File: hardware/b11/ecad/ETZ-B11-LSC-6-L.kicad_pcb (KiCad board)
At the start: 2 copper layers, 131.5 x 85.8 mm, 44 parts, among them SW1 Kailh_socket_PG1350, SW10 Kailh_socket_PG1350, SW11 Kailh_socket_PG1350, SW12 Kailh_socket_PG1350, SW13 Kailh_socket_PG1350, SW14 Kailh_socket_PG1350, SW15 Kailh_socket_PG1350, SW16 Kailh_socket_PG1350, SW17 Kailh_socket_PG1350, SW18 Kailh_socket_PG1350, SW19 Kailh_socket_PG1350, SW2 Kailh_socket_PG1350, SW20 Kailh_socket_PG1350, SW21 Kailh_socket_PG1350, SW22 Kailh_socket_PG1350, SW3 Kailh_socket_PG1350, SW4 Kailh_socket_PG1350, SW5 Kailh_socket_PG1350, SW6 Kailh_socket_PG1350, SW7 Kailh_socket_PG1350, SW8 Kailh_socket_PG1350, SW9 Kailh_socket_PG1350

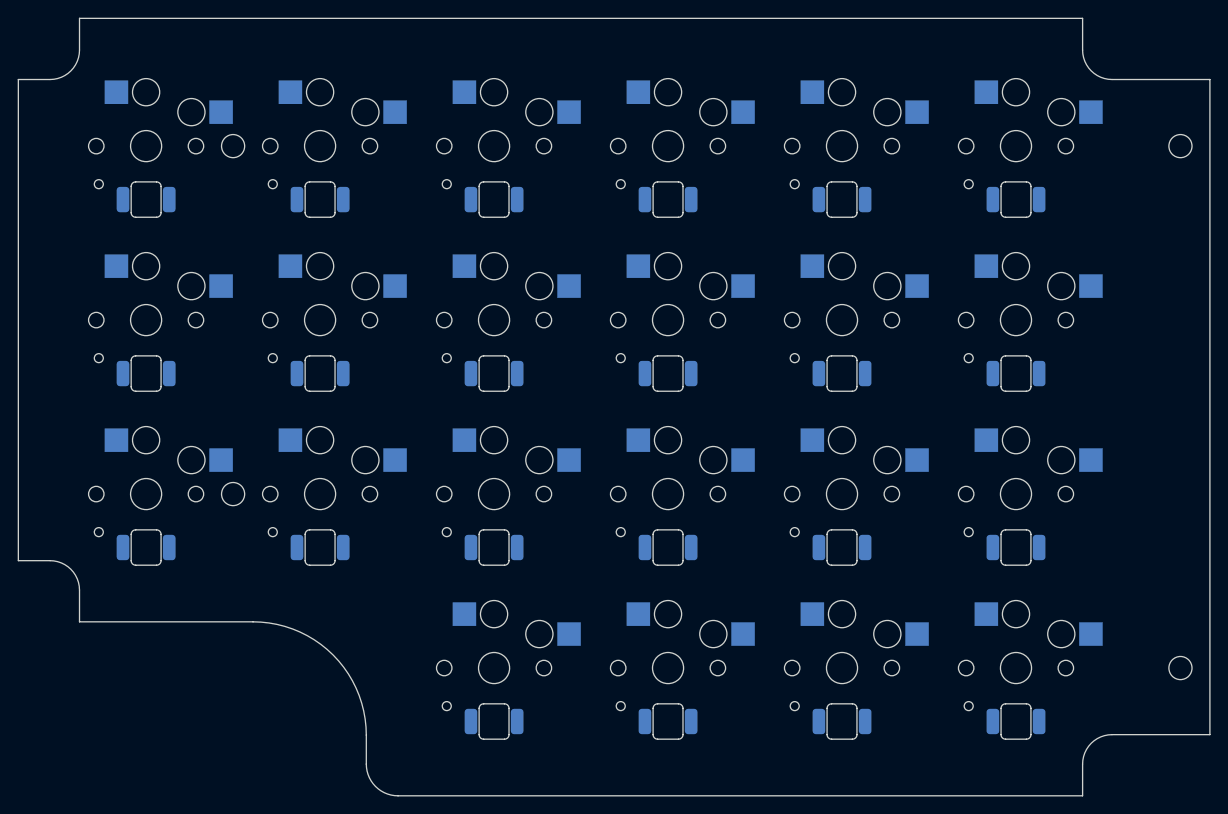
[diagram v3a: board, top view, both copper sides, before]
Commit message: fix(hardware/b11): fix switch socket placement, 3D models, and submodule pins
- Pin MX_V2 submodule to ab59b57 (before upstream "topside pads" change that
  moved SMD pads to F.Cu — old commit has correct B.Cu pads natively)
- Fix SWIG type-registry corruption in both switch placement scripts by
  pre-loading all footprint instances and caching pad refs before LoadBoard()
- Fix LP script: add make_patched_lib to rewrite Choc socket 3D model path
  to absolute path and convert old (at ...) inch offset to (offset ...) mm
  format — KiCad 9 was multiplying the old format by 25.4, placing model
  127mm off-center
- Regenerate all 8 carrier PCBs with updated board outlines (LSC-6 mounting
  hole positions) and correctly placed switches + LEDs

Co-Authored-By: Claude Sonnet 4.6 <noreply@anthropic.com>
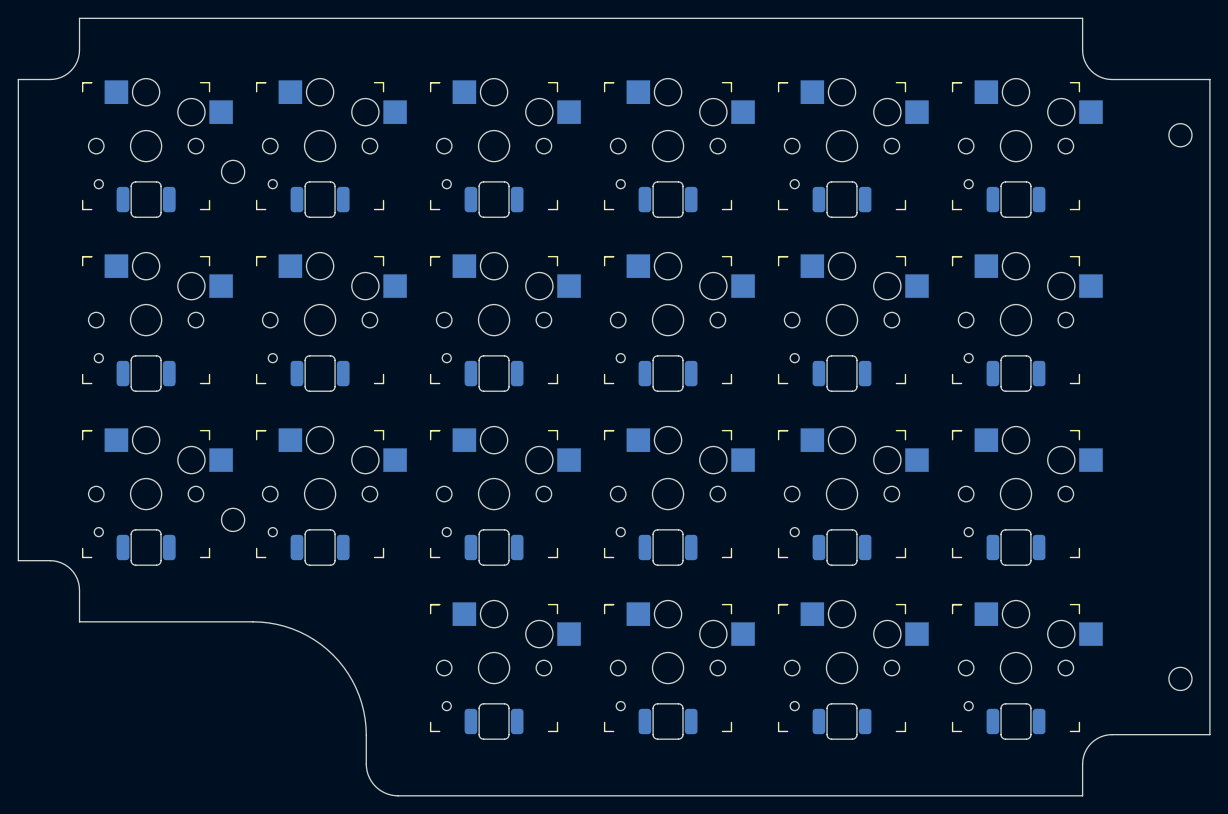
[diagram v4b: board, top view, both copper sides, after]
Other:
- outline, holes or cut-outs redrawn

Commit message: fix(hardware/b11): adjust LED offset to 5.0mm and regenerate all carrier PCBs
Reduces south-facing LED offset from 5.9mm to 5.0mm (closer to the
standard 5.08mm switch-to-LED spacing). All 8 carrier PCBs regenerated.

Co-Authored-By: Claude Sonnet 4.6 <noreply@anthropic.com>
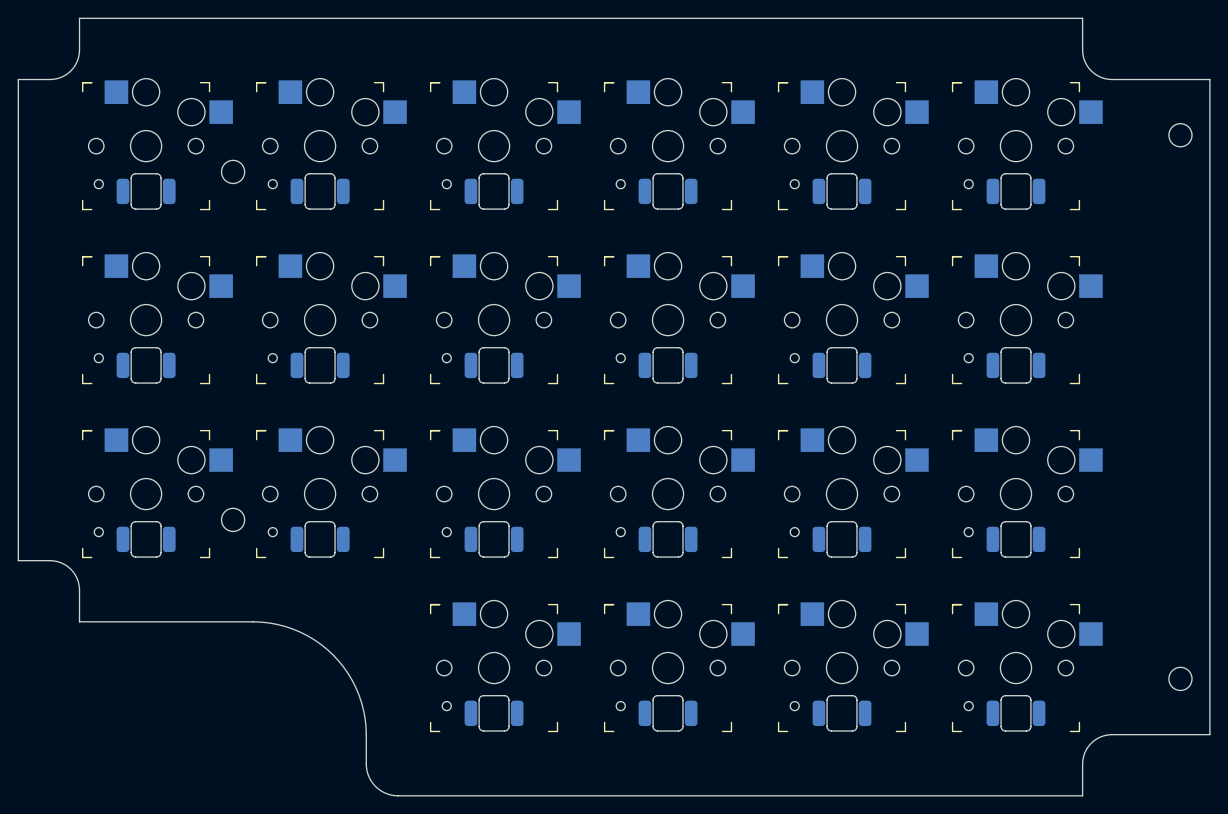
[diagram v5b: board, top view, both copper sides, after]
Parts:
- moved LED13 0.90 mm to (96.8, 116.7)
- moved LED14 0.90 mm to (116.0, 116.7)
- moved LED15 0.90 mm to (135.2, 116.7)
- moved LED16 0.90 mm to (154.4, 116.7)
- moved LED17 0.90 mm to (173.6, 116.7)
- moved LED18 0.90 mm to (192.8, 116.7)
- moved LED1 0.90 mm to (96.8, 78.3)
- moved LED10 0.90 mm to (154.4, 97.5)
- moved LED11 0.90 mm to (173.6, 97.5)
- moved LED12 0.90 mm to (192.8, 97.5)
- moved LED19 0.90 mm to (135.2, 135.9)
- moved LED2 0.90 mm to (116.0, 78.3)
- moved LED20 0.90 mm to (154.4, 135.9)
- moved LED21 0.90 mm to (173.6, 135.9)
- moved LED22 0.90 mm to (192.8, 135.9)
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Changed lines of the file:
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@@
 	(footprint "LED_SMD_6028_BackMount"
 		(layer "B.Cu")
-		(at 135.25 117.6)
+		(at 135.25 116.699999)
 		(descr "SMD 6028 back-paste reverse-mount LED, 5.88x2.80mm body, 3.20mm lens, slot 3.3x6.2mm")
 		(tags "LED SMD 6028 reverse-mount back-paste backlighting Choc")
@@
 	(footprint "LED_SMD_6028_BackMount"
 		(layer "B.Cu")
-		(at 135.25 98.4)
+		(at 135.25 78.3)
 		(descr "SMD 6028 back-paste reverse-mount LED, 5.88x2.80mm body, 3.20mm lens, slot 3.3x6.2mm")
 		(tags "LED SMD 6028 reverse-mount back-paste backlighting Choc")
-		(property "Reference" "LED9"
+		(property "Reference" "LED3"
 			(at 0 -2 0)
 			(layer "B.Fab")
@@
 	(footprint "LED_SMD_6028_BackMount"
 		(layer "B.Cu")
-		(at 96.85 98.4)
+		(at 192.85 135.899999)
 		(descr "SMD 6028 back-paste reverse-mount LED, 5.88x2.80mm body, 3.20mm lens, slot 3.3x6.2mm")
 		(tags "LED SMD 6028 reverse-mount back-paste backlighting Choc")
-		(property "Reference" "LED7"
+		(property "Reference" "LED22"
 			(at 0 -2 0)
 			(layer "B.Fab")
@@
 	(footprint "LED_SMD_6028_BackMount"
 		(layer "B.Cu")
-		(at 173.649999 117.6)
+		(at 173.649999 78.3)
 		(descr "SMD 6028 back-paste reverse-mount LED, 5.88x2.80mm body, 3.20mm lens, slot 3.3x6.2mm")
 		(tags "LED SMD 6028 reverse-mount back-paste backlighting Choc")
-		(property "Reference" "LED17"
+		(property "Reference" "LED5"
 			(at 0 -2 0)
 			(layer "B.Fab")
@@
 	(footprint "LED_SMD_6028_BackMount"
 		(layer "B.Cu")
-		(at 173.649999 136.799999)
+		(at 116.05 97.5)
 		(descr "SMD 6028 back-paste reverse-mount LED, 5.88x2.80mm body, 3.20mm lens, slot 3.3x6.2mm")
 		(tags "LED SMD 6028 reverse-mount back-paste backlighting Choc")
-		(property "Reference" "LED21"
+		(property "Reference" "LED8"
 			(at 0 -2 0)
 			(layer "B.Fab")
@@
 	(footprint "LED_SMD_6028_BackMount"
 		(layer "B.Cu")
-		(at 192.85 136.799999)
+		(at 116.05 78.3)
 		(descr "SMD 6028 back-paste reverse-mount LED, 5.88x2.80mm body, 3.20mm lens, slot 3.3x6.2mm")
 		(tags "LED SMD 6028 reverse-mount back-paste backlighting Choc")
-		(property "Reference" "LED22"
+		(property "Reference" "LED2"
 			(at 0 -2 0)
 			(layer "B.Fab")
@@
 	(footprint "LED_SMD_6028_BackMount"
 		(layer "B.Cu")
-		(at 192.85 79.2)
+		(at 173.649999 97.5)
 		(descr "SMD 6028 back-paste reverse-mount LED, 5.88x2.80mm body, 3.20mm lens, slot 3.3x6.2mm")
 		(tags "LED SMD 6028 reverse-mount back-paste backlighting Choc")
-		(property "Reference" "LED6"
+		(property "Reference" "LED11"
 			(at 0 -2 0)
 			(layer "B.Fab")
@@
 	(footprint "LED_SMD_6028_BackMount"
 		(layer "B.Cu")
-		(at 116.05 98.4)
+		(at 154.45 116.699999)
 		(descr "SMD 6028 back-paste reverse-mount LED, 5.88x2.80mm body, 3.20mm lens, slot 3.3x6.2mm")
 		(tags "LED SMD 6028 reverse-mount back-paste backlighting Choc")
-		(property "Reference" "LED8"
+		(property "Reference" "LED16"
 			(at 0 -2 0)
 			(layer "B.Fab")
@@
 	(footprint "LED_SMD_6028_BackMount"
 		(layer "B.Cu")
-		(at 96.85 117.6)
+		(at 173.649999 116.699999)
 		(descr "SMD 6028 back-paste reverse-mount LED, 5.88x2.80mm body, 3.20mm lens, slot 3.3x6.2mm")
 		(tags "LED SMD 6028 reverse-mount back-paste backlighting Choc")
-		(property "Reference" "LED13"
+		(property "Reference" "LED17"
 			(at 0 -2 0)
 			(layer "B.Fab")
@@
 	(footprint "LED_SMD_6028_BackMount"
 		(layer "B.Cu")
-		(at 154.45 79.2)
+		(at 154.45 97.5)
 		(descr "SMD 6028 back-paste reverse-mount LED, 5.88x2.80mm body, 3.20mm lens, slot 3.3x6.2mm")
 		(tags "LED SMD 6028 reverse-mount back-paste backlighting Choc")
-		(property "Reference" "LED4"
+		(property "Reference" "LED10"
 			(at 0 -2 0)
 			(layer "B.Fab")
@@
 	(footprint "LED_SMD_6028_BackMount"
 		(layer "B.Cu")
-		(at 192.85 98.4)
+		(at 135.25 135.899999)
 		(descr "SMD 6028 back-paste reverse-mount LED, 5.88x2.80mm body, 3.20mm lens, slot 3.3x6.2mm")
 		(tags "LED SMD 6028 reverse-mount back-paste backlighting Choc")
-		(property "Reference" "LED12"
+		(property "Reference" "LED19"
 			(at 0 -2 0)
 			(layer "B.Fab")
@@
 	(footprint "LED_SMD_6028_BackMount"
 		(layer "B.Cu")
-		(at 116.05 117.6)
+		(at 96.85 78.3)
 		(descr "SMD 6028 back-paste reverse-mount LED, 5.88x2.80mm body, 3.20mm lens, slot 3.3x6.2mm")
 		(tags "LED SMD 6028 reverse-mount back-paste backlighting Choc")
-		(property "Reference" "LED14"
+		(property "Reference" "LED1"
 			(at 0 -2 0)
 			(layer "B.Fab")
@@
 	(footprint "LED_SMD_6028_BackMount"
 		(layer "B.Cu")
-		(at 116.05 79.2)
+		(at 154.45 135.899999)
 		(descr "SMD 6028 back-paste reverse-mount LED, 5.88x2.80mm body, 3.20mm lens, slot 3.3x6.2mm")
 		(tags "LED SMD 6028 reverse-mount back-paste backlighting Choc")
-		(property "Reference" "LED2"
+		(property "Reference" "LED20"
 			(at 0 -2 0)
 			(layer "B.Fab")
@@
 	(footprint "LED_SMD_6028_BackMount"
 		(layer "B.Cu")
-		(at 135.25 79.2)
+		(at 192.85 78.3)
 		(descr "SMD 6028 back-paste reverse-mount LED, 5.88x2.80mm body, 3.20mm lens, slot 3.3x6.2mm")
 		(tags "LED SMD 6028 reverse-mount back-paste backlighting Choc")
-		(property "Reference" "LED3"
+		(property "Reference" "LED6"
 			(at 0 -2 0)
 			(layer "B.Fab")
@@
 	(footprint "LED_SMD_6028_BackMount"
 		(layer "B.Cu")
-		(at 135.25 136.799999)
+		(at 192.85 97.5)
 		(descr "SMD 6028 back-paste reverse-mount LED, 5.88x2.80mm body, 3.20mm lens, slot 3.3x6.2mm")
 		(tags "LED SMD 6028 reverse-mount back-paste backlighting Choc")
-		(property "Reference" "LED19"
+		(property "Reference" "LED12"
 			(at 0 -2 0)
 			(layer "B.Fab")
@@
 	(footprint "LED_SMD_6028_BackMount"
 		(layer "B.Cu")
-		(at 154.45 117.6)
+		(at 96.85 97.5)
 		(descr "SMD 6028 back-paste reverse-mount LED, 5.88x2.80mm body, 3.20mm lens, slot 3.3x6.2mm")
 		(tags "LED SMD 6028 reverse-mount back-paste backlighting Choc")
-		(property "Reference" "LED16"
+		(property "Reference" "LED7"
 			(at 0 -2 0)
 			(layer "B.Fab")
@@
 	(footprint "LED_SMD_6028_BackMount"
 		(layer "B.Cu")
-		(at 192.85 117.6)
+		(at 192.85 116.699999)
 		(descr "SMD 6028 back-paste reverse-mount LED, 5.88x2.80mm body, 3.20mm lens, slot 3.3x6.2mm")
 		(tags "LED SMD 6028 reverse-mount back-paste backlighting Choc")
@@
 	(footprint "LED_SMD_6028_BackMount"
 		(layer "B.Cu")
-		(at 154.45 136.799999)
+		(at 96.85 116.699999)
 		(descr "SMD 6028 back-paste reverse-mount LED, 5.88x2.80mm body, 3.20mm lens, slot 3.3x6.2mm")
 		(tags "LED SMD 6028 reverse-mount back-paste backlighting Choc")
-		(property "Reference" "LED20"
+		(property "Reference" "LED13"
 			(at 0 -2 0)
 			(layer "B.Fab")
@@
 	(footprint "LED_SMD_6028_BackMount"
 		(layer "B.Cu")
-		(at 173.649999 79.2)
+		(at 154.45 78.3)
 		(descr "SMD 6028 back-paste reverse-mount LED, 5.88x2.80mm body, 3.20mm lens, slot 3.3x6.2mm")
 		(tags "LED SMD 6028 reverse-mount back-paste backlighting Choc")
-		(property "Reference" "LED5"
+		(property "Reference" "LED4"
 			(at 0 -2 0)
 			(layer "B.Fab")
@@
 	(footprint "LED_SMD_6028_BackMount"
 		(layer "B.Cu")
-		(at 96.85 79.2)
+		(at 173.649999 135.899999)
 		(descr "SMD 6028 back-paste reverse-mount LED, 5.88x2.80mm body, 3.20mm lens, slot 3.3x6.2mm")
 		(tags "LED SMD 6028 reverse-mount back-paste backlighting Choc")
-		(property "Reference" "LED1"
+		(property "Reference" "LED21"
 			(at 0 -2 0)
 			(layer "B.Fab")
@@
 	(footprint "LED_SMD_6028_BackMount"
 		(layer "B.Cu")
-		(at 154.45 98.4)
+		(at 116.05 116.699999)
 		(descr "SMD 6028 back-paste reverse-mount LED, 5.88x2.80mm body, 3.20mm lens, slot 3.3x6.2mm")
 		(tags "LED SMD 6028 reverse-mount back-paste backlighting Choc")
-		(property "Reference" "LED10"
+		(property "Reference" "LED14"
 			(at 0 -2 0)
 			(layer "B.Fab")
@@
 	(footprint "LED_SMD_6028_BackMount"
 		(layer "B.Cu")
-		(at 173.649999 98.4)
+		(at 135.25 97.5)
 		(descr "SMD 6028 back-paste reverse-mount LED, 5.88x2.80mm body, 3.20mm lens, slot 3.3x6.2mm")
 		(tags "LED SMD 6028 reverse-mount back-paste backlighting Choc")
-		(property "Reference" "LED11"
+		(property "Reference" "LED9"
 			(at 0 -2 0)
 			(layer "B.Fab")
